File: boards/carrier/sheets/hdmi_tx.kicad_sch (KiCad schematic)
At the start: 14 parts, among them J1 HDMI-019S, U1 TPD12S016PWR, U2 24LC256T-I/SN

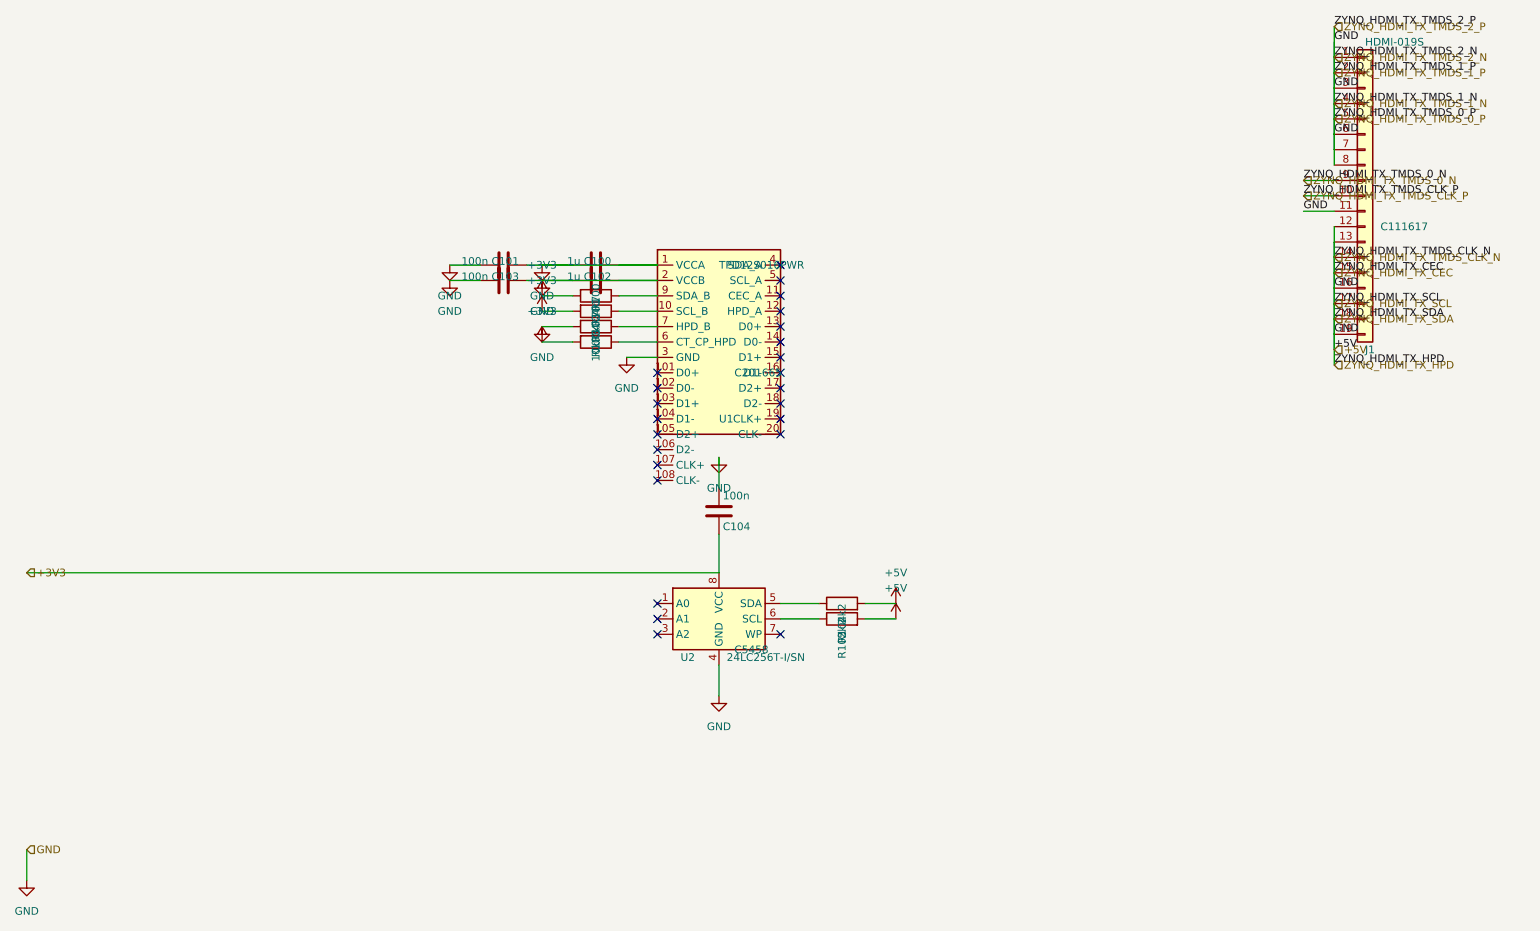
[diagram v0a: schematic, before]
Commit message: Track 2c: exhaustive audit of video / network refcircuits
TPD12S016_TX/RX: rewrote header with full PW pin map; removed spurious
                 4.7k I2C and 100k HPD external pull-ups (all integrated
                 per DS Sec 7.3.9, 7.3.15); kept only the V_CCA + V_CC5V
                 100nF caps and the CT_HPD 10k pull-up that DS Fig 15
                 actually requires; added pin_net_overrides mapping the
                 symbol's VCCA/VCCB to +3V3 / +5V (TX) or +3V3 /
                 ZYNQ_HDMI_RX_5V_SENSE (RX); expanded layout_notes with
                 the five DS Sec 10 layout rules.
HDMI_A:          replaced the misplaced 10k CEC + 2k2 DDC pull-ups with
                 a 1uF + 100nF VBUS bulk/bypass per HDMI 1.4 Sec 4.2.7;
                 kept the 1M + 100nF shield-to-CHASSIS_GND discharge
                 network; added the SOFNG HDMI-019S pin table from
                 sheet 2 of the datasheet; layout_notes now cite HDMI
                 1.4 Sec 4.2.3 + TPD12S016 DS Sec 10.1 explicitly.
24LC256:         clarified header (board-ID role on +3V3 system bus,
                 strap A2=A1=A0=0 -> addr 0x50); kept the 100nF VCC
                 cap + the 4k7 SDA/SCL pull-ups (this is the canonical
                 system-I2C bus pull-up donor); added I2C-bus-spec
                 layout note for the 400 pF capacitance budget.
24LC256_EDID:    corrected the I2C straps - HDMI 1.4 Sec 8.1.4 / VESA
                 E-DDC mandate A2=A1=A0=0 (addr 0x50), so A1 must be
                 GND not +5V; removed the duplicate 2k2 DDC pull-ups
                 (TPD12S016 SDA_B/SCL_B already pull up internally
                 1.75k to 5V_OUT); explicit layout rule that V_CC must
                 share the same +5V node as TPD12S016 5V_OUT.
HX5008NLT:       factored Bob Smith generation into a helper so each
                 of the four CT_PAIR0..3 lines gets one 75R + one
                 1nF/2kV consistently; expanded header with full per-
                 channel pi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
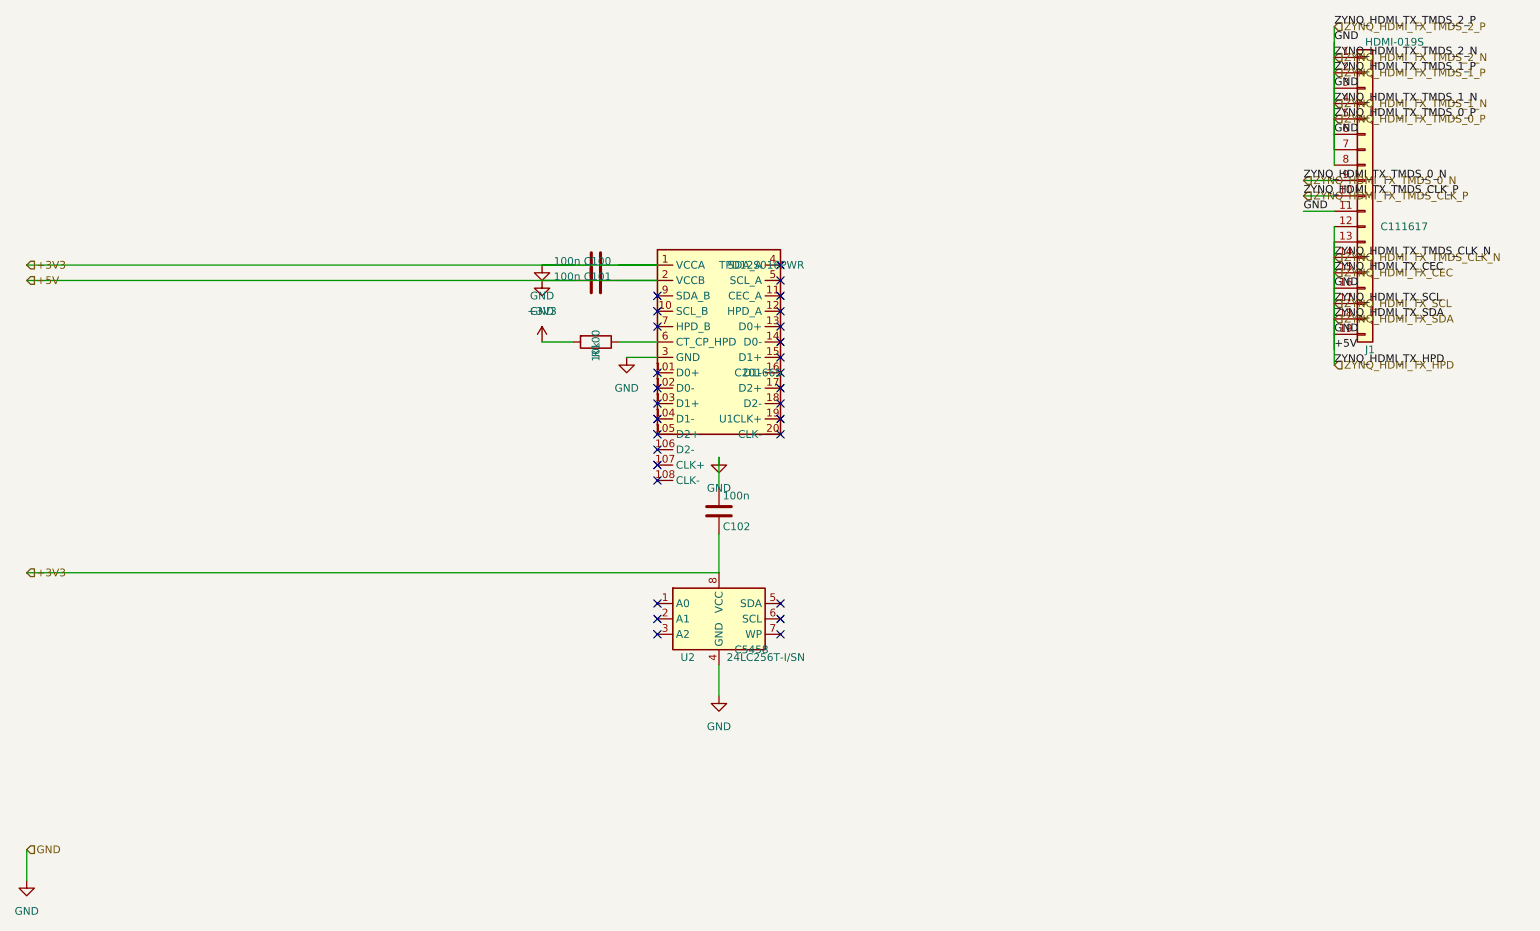
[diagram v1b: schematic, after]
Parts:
- removed C103, C104: 100n, Capacitor_SMD:C_0402_1005Metric, symbol Device:C
- removed R101: 4k7, Resistor_SMD:R_0402_1005Metric, symbol Device:R
- removed R102: 100k, Resistor_SMD:R_0402_1005Metric, symbol Device:R
- removed R103: 10k, Resistor_SMD:R_0402_1005Metric, symbol Device:R
- removed R104, R105: 2k2, Resistor_SMD:R_0402_1005Metric, symbol Device:R
- C100, C102: value 1u -> 100n
- R100: value 4k7 -> 10k
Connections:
- net +5V is gone; now on net +3V3: C100.1, C100.2, C101.1, C101.2, C102.1, C102.2, J1.1 (Pin_1), J1.11 (Pin_11), J1.12 (Pin_12), J1.13 (Pin_13), J1.14 (Pin_14), J1.15 (Pin_15), J1.16 (Pin_16), J1.17 (Pin_17), J1.18 (Pin_18), J1.19 (Pin_19), J1.2 (Pin_2), J1.3 (Pin_3), J1.4 (Pin_4), J1.5 (Pin_5), J1.6 (Pin_6), J1.7 (Pin_7), J1.8 (Pin_8), U1.1 (VCCA), U1.2 (VCCB), U1.3 (GND), U2.4 (GND)
- net at U1.6 (CT_CP_HPD): now also R100.1
- net at U1.9 (SDA_B): no longer R100.1
- no-connect marks 24 -> 29
